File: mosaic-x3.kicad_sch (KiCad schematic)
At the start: 0 parts

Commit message: schematic designs done
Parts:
- added C1: 1000uF, symbol Device:C_Polarized
- added C2, C5: 10uF, symbol Device:C
- added C3: 22uF, symbol Device:C
- added C4, C7, C8: 0.1uF, symbol Device:C
- added C6: 1uF, symbol Device:C
- added D1: D_Schottky, symbol Device:D_Schottky
- added F1: 6A, symbol Device:Polyfuse
- added J1: Barrel_Jack, symbol Connector:Barrel_Jack
- added J2: USB_C_Receptacle_USB2.0_14P, symbol Connector:USB_C_Receptacle_USB2.0_14P
- added J3: LED_STRIP_HEAD, symbol Connector_Generic:Conn_01x03
- added J4: PWR_INJ_1, symbol Connector_Generic:Conn_01x02
- added J5: PWR_INJ_2, symbol Connector_Generic:Conn_01x02
- added J6: PWR_INJ_3, symbol Connector_Generic:Conn_01x02
- added R1, R2: 10k, symbol Device:R
- added R3, R4: 5.1k, symbol Device:R
- added R5: 330, symbol Device:R
- added SW1: SW_SPST, symbol Switch:SW_SPST
- added SW2: RESET, symbol Switch:SW_Push
- added SW3: BOOT, symbol Switch:SW_Push
- added U1: AMS1117-3.3, Package_TO_SOT_SMD:SOT-223-3_TabPin2, symbol Regulator_Linear:AMS1117-3.3
- added U2: ESP32-S3-WROOM-1, RF_Module:ESP32-S3-WROOM-1, symbol RF_Module:ESP32-S3-WROOM-1
- added U3: 74AHCT125, symbol 74xx:74AHCT125
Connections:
- new net: R5.2, U3.3
- new net: J2.B5 (CC2), R3.2
- new net: F1.2, SW1.1 (A)
- new net: D1.2 (A), SW1.2 (B)
- new net: F1.1, J1.1
- new net: C2.2, C3.2
- new net: J2.A5 (CC1), R4.2
- new net: J2.A4 (VBUS), J2.A9 (VBUS), J2.B4 (VBUS), J2.B9 (VBUS)
- new net +3V3: C3.1, C4.1, C5.1, R1.1, R2.1, U1.2 (VO), U2.2 (3V3)
- new net +5V: C1.1, C2.1, C8.1, D1.1 (K), J3.1 (Pin_1), J4.1 (Pin_1), J5.1 (Pin_1), J6.1 (Pin_1), U1.3 (VI), U3.10, U3.13, U3.14 (VCC), U3.4
- new net EN: C6.1, R1.2, SW2.2, U2.3 (EN)
- new net GND: C1.2, C4.2, C5.2, C6.2, C7.2, C8.2, J1.2, J2.A1 (GND), J2.A12 (GND), J2.B1 (GND), J2.B12 (GND), J2.SH (SHIELD), J3.2 (Pin_2), J4.2 (Pin_2), J5.2 (Pin_2), J6.2 (Pin_2), R3.1, R4.1, SW2.1, SW3.1, U1.1 (GND), U2.1 (GND), U2.40 (GND), U2.41 (GND), U3.1, U3.12, U3.5, U3.7 (GND), U3.9
- new net IO0: C7.1, R2.2, SW3.2, U2.27 (IO0)
- new net LED_DATA_3V3: U2.31 (IO38), U3.2
- new net LED_DATA_5V: J3.3 (Pin_3), R5.1
- new net USB_DM: J2.A7 (D-), J2.B7 (D-), U2.13 (USB_D-)
- new net USB_DP: J2.A6 (D+), J2.B6 (D+), U2.14 (USB_D+)
- no-connect marks 0 -> 36
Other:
- note added: "June 2nd, 2026"
- note added: "Mosaic - a github activity visualizer"
- note added: "Mosaic-X3 schematics (v1): 26 weeks x 7 days (6 months) = 182 LEDs recommended: 60 LEDs/m WS2812B strip Firmware NUM_LEDS = 182"

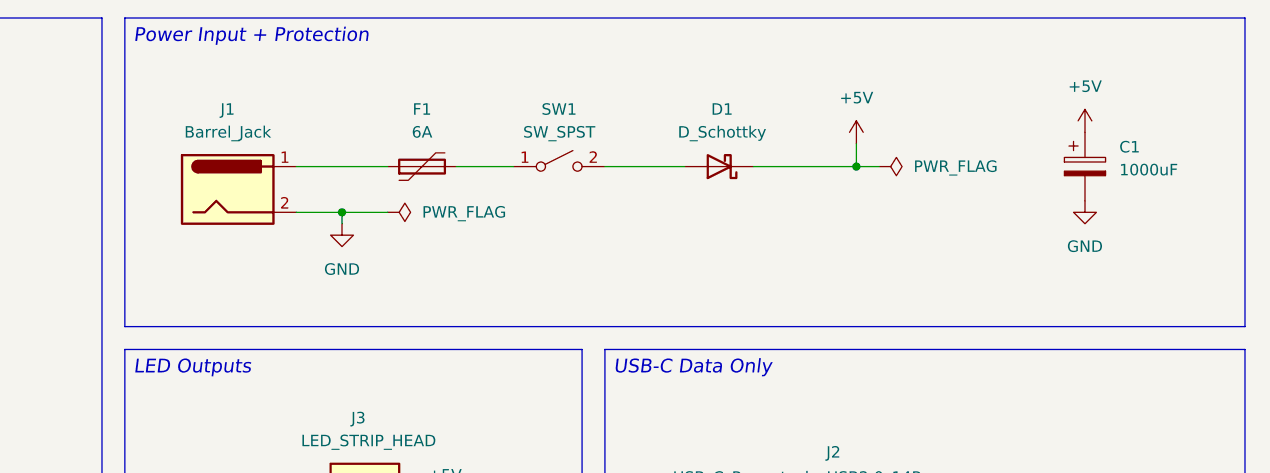
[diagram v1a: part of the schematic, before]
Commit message: update: working with footprints & PCB + added a 3d model for usb c
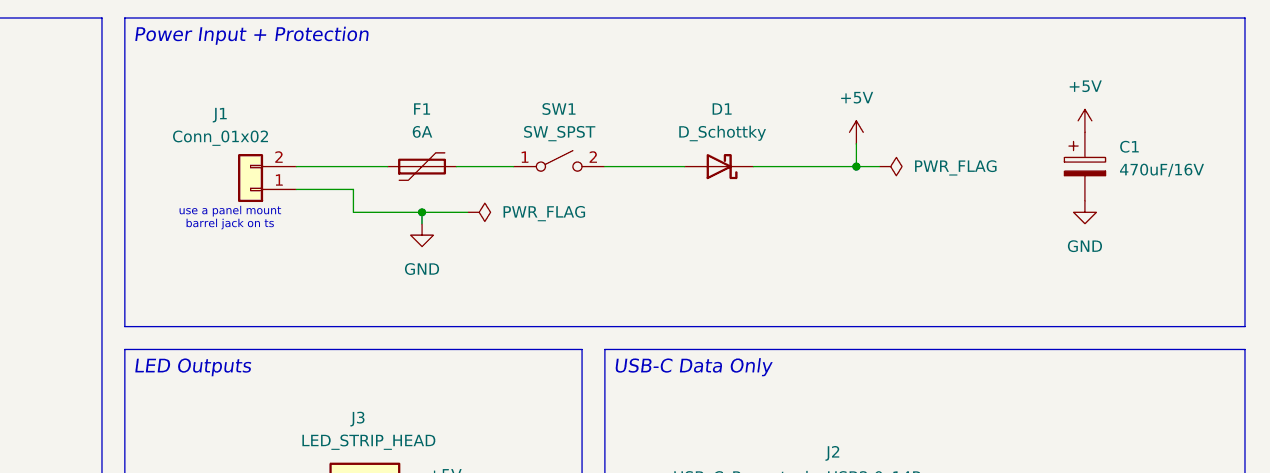
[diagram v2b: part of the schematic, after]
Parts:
- removed J1: Barrel_Jack, symbol Connector:Barrel_Jack
- added J1: Conn_01x02, TerminalBlock_Phoenix:TerminalBlock_Phoenix_MKDS-1-2-3.81_1x02_P3.81mm_Horizontal, symbol Connector_Generic:Conn_01x02
- C1: value 1000uF -> 470uF/16V; footprint (none) -> Capacitor_THT:CP_Radial_D8.0mm_P3.50mm
- C2, C3, C4, C5, C6, C7, C8: footprint (none) -> Capacitor_SMD:C_0805_2012Metric
- D1: footprint (none) -> Diode_SMD:D_SMA
- F1: footprint (none) -> Fuse:Fuse_1812_4532Metric
- J2: footprint (none) -> Connector_USB:USB_C_Receptacle_HRO_TYPE-C-31-M-12
- J3: footprint (none) -> Connector_JST:JST_XH_S3B-XH-A_1x03_P2.50mm_Horizontal
- J4, J5, J6: footprint (none) -> Connector_JST:JST_XH_S2B-XH-A_1x02_P2.50mm_Horizontal
- R1, R2, R3, R4, R5: footprint (none) -> Resistor_SMD:R_0805_2012Metric
- SW1: footprint (none) -> Button_Switch_THT:SW_Slide_SPDT_Angled_CK_OS102011MA1Q
- SW2, SW3: footprint (none) -> Button_Switch_THT:SW_PUSH_6mm
- U3: footprint (none) -> Package_SO:SOIC-14_3.9x8.7mm_P1.27mm
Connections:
- net GND: now also J1.1 (Pin_1)
- net at F1.1: now also J1.2 (Pin_2)
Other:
- note added: "use a panel mount barrel jack on ts"

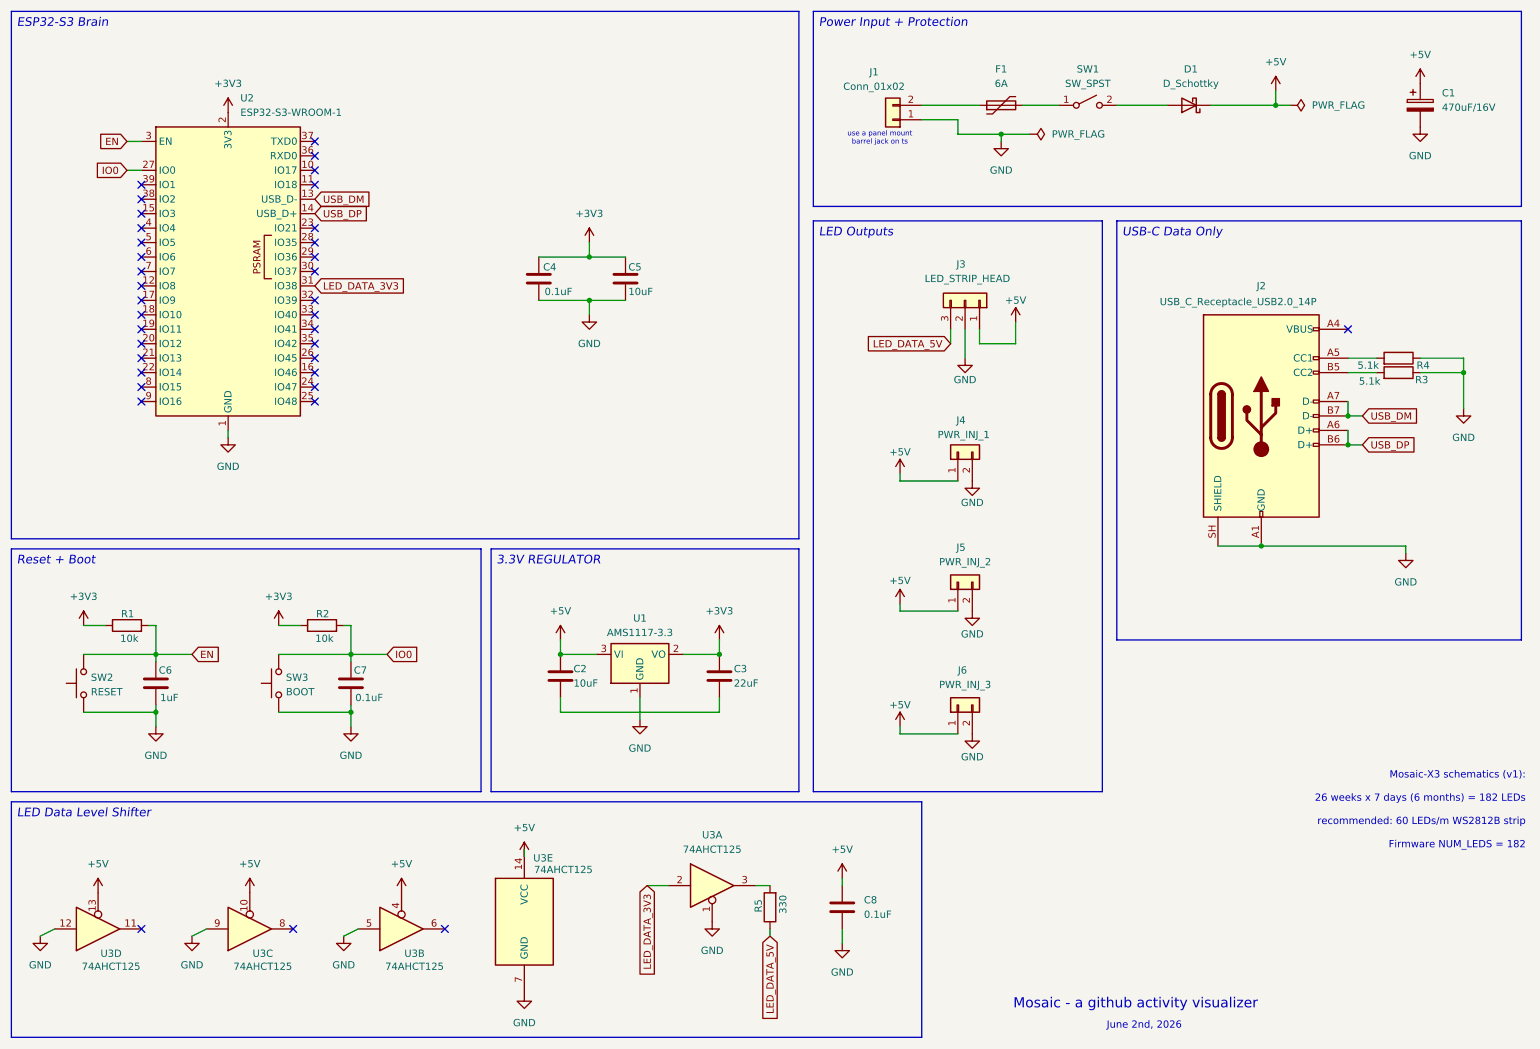
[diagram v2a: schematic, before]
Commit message: updated schematic and fixed erc errors
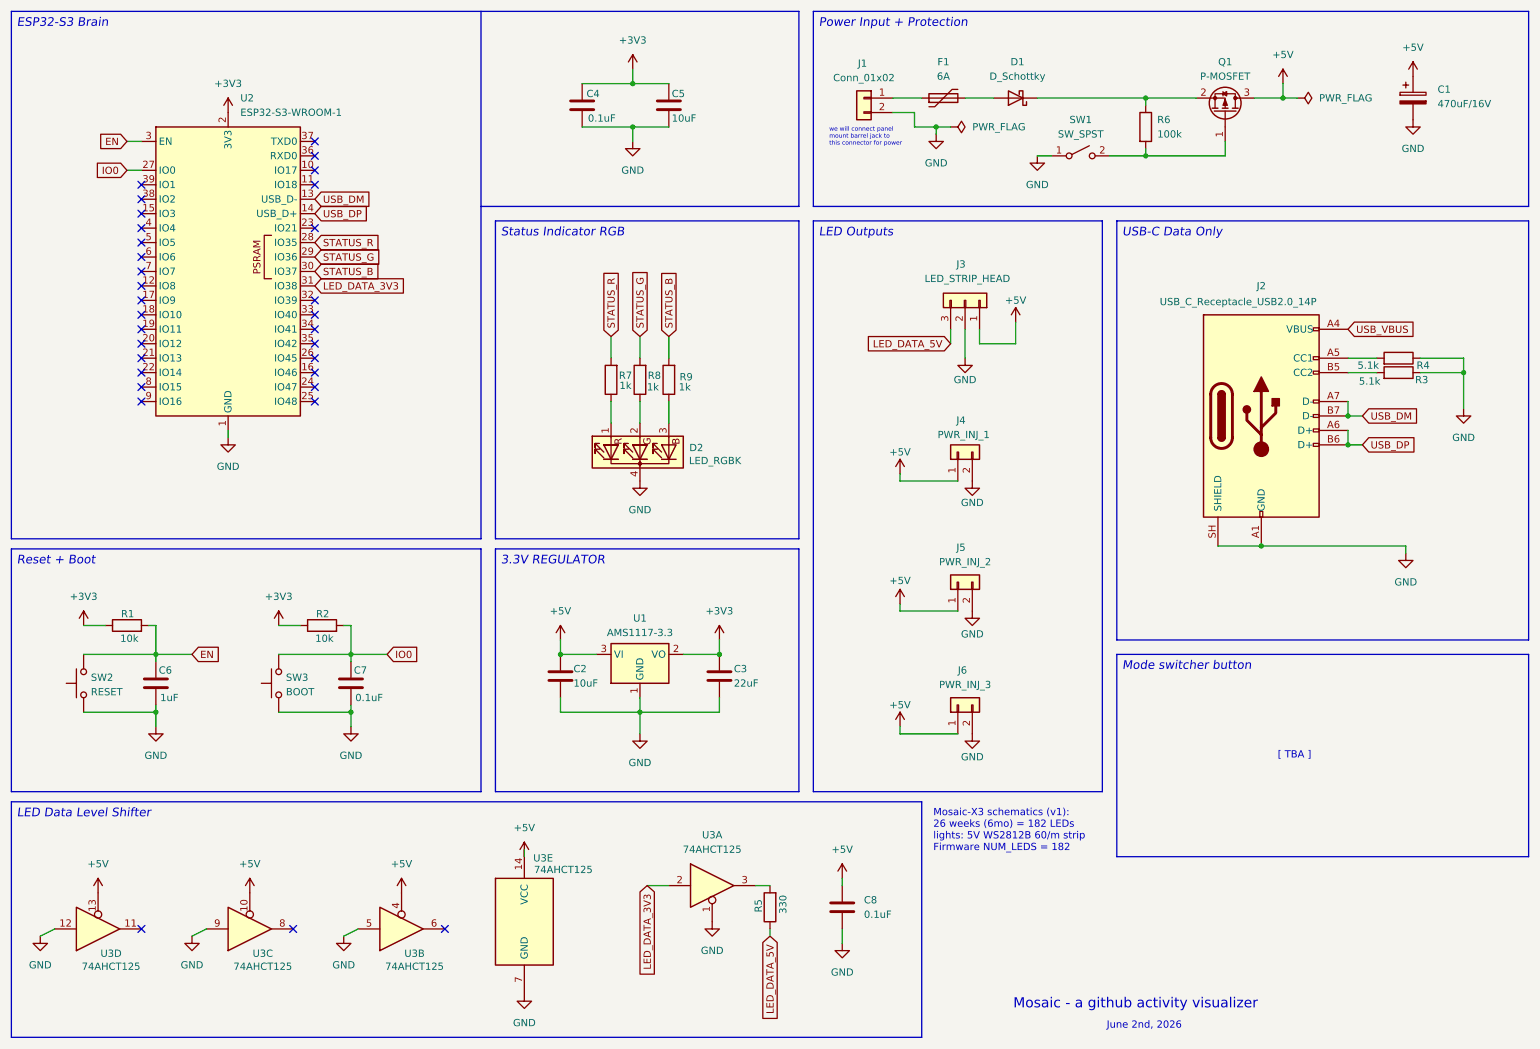
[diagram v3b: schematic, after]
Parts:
- added D2: LED_RGBK, LED_THT:LED_D5.0mm-4_RGB, symbol Device:LED_RGBK
- added Q1: P-MOSFET, Package_TO_SOT_SMD:SOT-223-3_TabPin2, symbol Transistor_FET:Q_PMOS_GSD
- added R6: 100k, Resistor_SMD:R_0805_2012Metric, symbol Device:R
- added R7, R8, R9: 1k, Resistor_SMD:R_0805_2012Metric_Pad1.20x1.40mm_HandSolder, symbol Device:R
- SW2, SW3: footprint Button_Switch_THT:SW_PUSH_6mm -> Button_Switch_SMD:SW_SPST_SKQG_WithStem
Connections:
- net +5V: now also Q1.3 (D); no longer D1.1 (K)
- net GND: now also C2.2, C3.2, J1.2 (Pin_2), SW1.1 (A), D2.4 (K); no longer J1.1 (Pin_1)
- net at F1.1: now also J1.1 (Pin_1); no longer J1.2 (Pin_2)
- net at F1.2: now also D1.2 (A); no longer SW1.1 (A)
- net at SW1.2 (B): now also Q1.1 (G), R6.2; no longer D1.2 (A)
- net STATUS_R: now reaches U2.28 (IO35)
- net STATUS_R: now also R7.2
- net STATUS_G: now reaches U2.29 (IO36)
- net STATUS_G: now also R8.2
- net STATUS_B: now reaches U2.30 (IO37)
- net STATUS_B: now also R9.2
- net USB_VBUS: now reaches J2.A4 (VBUS), J2.A9 (VBUS), J2.B4 (VBUS), J2.B9 (VBUS)
- new net: D2.1 (RA), R7.1
- new net: D2.2 (GA), R8.1
- new net: D2.3 (BA), R9.1
- new net: D1.1 (K), Q1.2 (S), R6.1
- no-connect marks 36 -> 32
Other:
- note added: "Mosaic-X3 schematics (v1): 26 weeks (6mo) = 182 LEDs lights: 5V WS2812B 60/m strip Firmware NUM_LEDS = 182"
- note added: "[ TBA ]"
- note added: "we will connect panel mount barrel jack to this connector for power"
- note removed: "Mosaic-X3 schematics (v1): 26 weeks x 7 days (6 months) = 182 LEDs recommended: 60 LEDs/m WS2812B strip Firmware NUM_LEDS = 182"
- note removed: "use a panel mount barrel jack on ts"
- moved on the sheet: C1, C4, C5, D1, F1, SW1

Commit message: finished w the pcb board
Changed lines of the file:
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@@
 	(text "[ TBA ]"
 		(exclude_from_sim no)
-		(at 240.792 146.05 0)
+		(at 243.332 146.812 0)
 		(effects
 			(font
